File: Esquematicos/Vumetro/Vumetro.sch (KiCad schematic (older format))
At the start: 14 parts

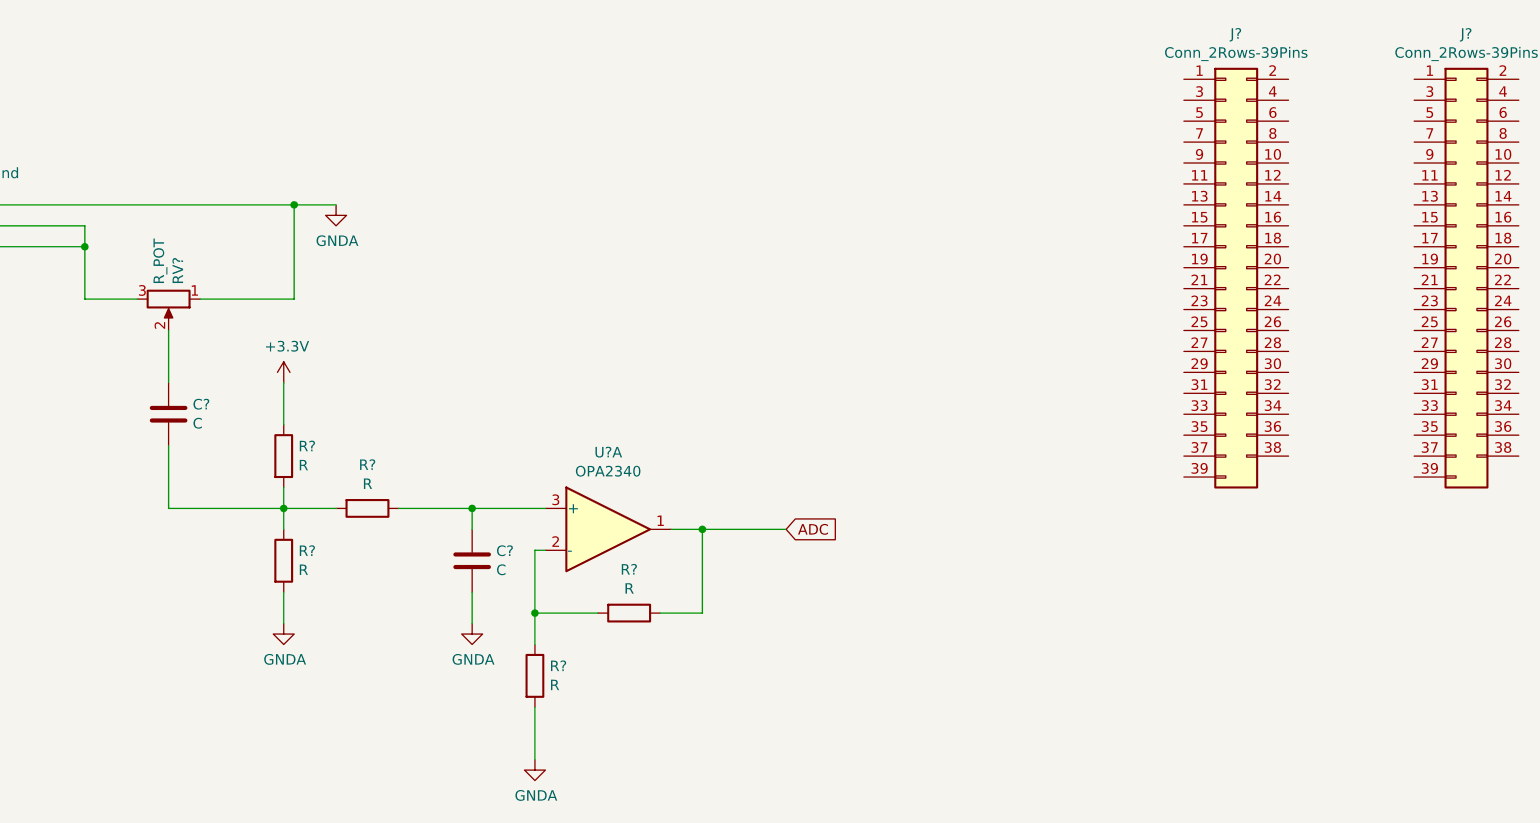
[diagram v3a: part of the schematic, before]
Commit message: Se agrega simulacion de esquematico
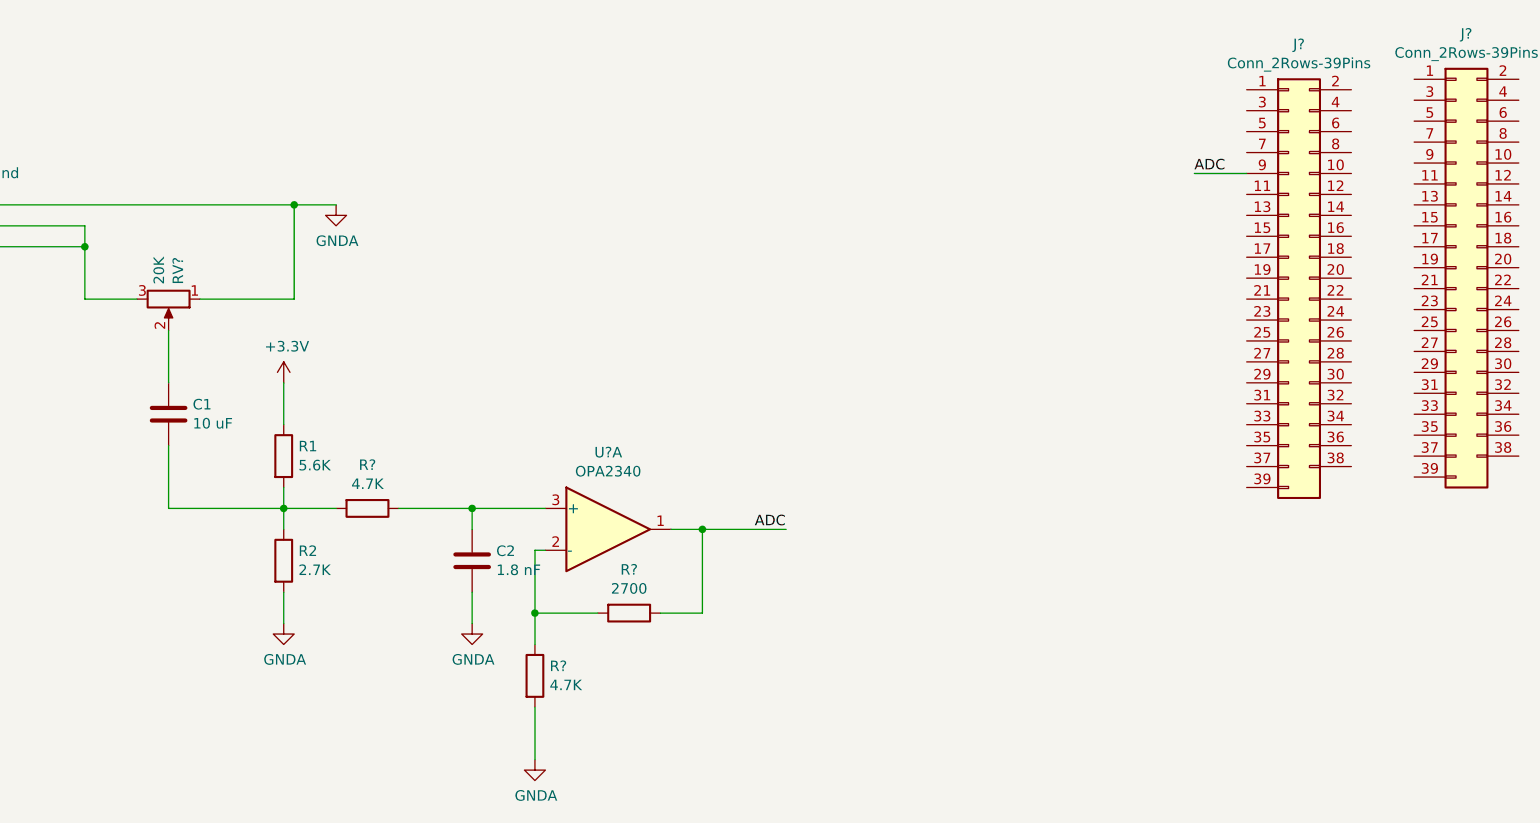
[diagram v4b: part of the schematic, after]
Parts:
- C1: renamed from C?; value C -> 10 uF
- C2: renamed from C?; value C -> 1.8 nF
- R1: renamed from R?; value R -> 5.6K
- R2: renamed from R?; value R -> 2.7K
- R? (x2): value R -> 4.7K
- R?: value R -> 2700
- RV?: value R_POT -> 20K
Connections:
- wire segments 30 -> 31
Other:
- moved on the sheet: J?
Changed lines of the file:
@@
 EESchema Schematic File Version 4
 LIBS:Vumetro-cache
-EELAYER 26 0
+EELAYER 29 0
 EELAYER END
 $Descr A4 11693 8268
@@
 $EndDescr
 $Comp
-L Device:R R?
+L Device:R R1
 U 1 1 5BD08240
 P 3400 2900
-F 0 "R?" H 3470 2946 50  0000 L CNN
-F 1 "R" H 3470 2855 50  0000 L CNN
+F 0 "R1" H 3470 2946 50  0000 L CNN
+F 1 "5.6K" H 3470 2855 50  0000 L CNN
 F 2 "" V 3330 2900 50  0001 C CNN
 F 3 "~" H 3400 2900 50  0001 C CNN
@@
 $EndComp
 $Comp
-L Device:R R?
+L Device:R R2
 U 1 1 5BD082FA
 P 3400 3400
-F 0 "R?" H 3470 3446 50  0000 L CNN
-F 1 "R" H 3470 3355 50  0000 L CNN
+F 0 "R2" H 3470 3446 50  0000 L CNN
+F 1 "2.7K" H 3470 3355 50  0000 L CNN
 F 2 "" V 3330 3400 50  0001 C CNN
 F 3 "~" H 3400 3400 50  0001 C CNN
@@
 $EndComp
 $Comp
-L power:+3.3V #PWR?
+L power:+3.3V #PWR0101
 U 1 1 5BD083BF
 P 3400 2550
-F 0 "#PWR?" H 3400 2400 50  0001 C CNN
+F 0 "#PWR0101" H 3400 2400 50  0001 C CNN
 F 1 "+3.3V" H 3415 2723 50  0000 C CNN
 F 2 "" H 3400 2550 50  0001 C CNN
@@
 $EndComp
 $Comp
-L power:GNDA #PWR?
+L power:GNDA #PWR0102
 U 1 1 5BD08B01
 P 3650 1700
-F 0 "#PWR?" H 3650 1450 50  0001 C CNN
+F 0 "#PWR0102" H 3650 1450 50  0001 C CNN
 F 1 "GNDA" H 3655 1527 50  0000 C CNN
 F 2 "" H 3650 1700 50  0001 C CNN
@@
 P 2850 2150
 F 0 "RV?" H 2780 2196 50  0000 R CNN
-F 1 "R_POT" H 2780 2105 50  0000 R CNN
+F 1 "20K" H 2780 2105 50  0000 R CNN
 F 2 "" H 2850 2150 50  0001 C CNN
 F 3 "~" H 2850 2150 50  0001 C CNN
@@
 Connection ~ 3400 3150
 $Comp
-L power:GNDA #PWR?
+L power:GNDA #PWR0103
 U 1 1 5BD0D7F2
 P 3400 3700
-F 0 "#PWR?" H 3400 3450 50  0001 C CNN
+F 0 "#PWR0103" H 3400 3450 50  0001 C CNN
 F 1 "GNDA" H 3405 3527 50  0000 C CNN
 F 2 "" H 3400 3700 50  0001 C CNN
@@
 $EndComp
 $Comp
-L Device:C C?
+L Device:C C2
 U 1 1 5BD1B29A
 P 4300 3400
-F 0 "C?" H 4415 3446 50  0000 L CNN
-F 1 "C" H 4415 3355 50  0000 L CNN
+F 0 "C2" H 4415 3446 50  0000 L CNN
+F 1 "1.8 nF" H 4415 3355 50  0000 L CNN
 F 2 "" H 4338 3250 50  0001 C CNN
 F 3 "~" H 4300 3400 50  0001 C CNN
@@
 $EndComp
 $Comp
-L power:GNDA #PWR?
+L power:GNDA #PWR0104
 U 1 1 5BD1B343
 P 4300 3700
-F 0 "#PWR?" H 4300 3450 50  0001 C CNN
+F 0 "#PWR0104" H 4300 3450 50  0001 C CNN
 F 1 "GNDA" H 4305 3527 50  0000 C CNN
 F 2 "" H 4300 3700 50  0001 C CNN
@@
 P 3800 3150
 F 0 "R?" V 3593 3150 50  0000 C CNN
-F 1 "R" V 3684 3150 50  0000 C CNN
+F 1 "4.7K" V 3684 3150 50  0000 C CNN
 F 2 "" V 3730 3150 50  0001 C CNN
 F 3 "~" H 3800 3150 50  0001 C CNN
@@
 Wire Wire Line
 	4300 3150 4300 3250
-Text GLabel 5800 3250 2    50   Input ~ 0
-ADC
 Wire Wire Line
 	3400 3550 3400 3700
@@
 L Connector_Generic:Conn_2Rows-39Pins J?
 U 1 1 5BD1C88D
-P 7900 2000
-F 0 "J?" H 7950 3117 50  0000 C CNN
-F 1 "Conn_2Rows-39Pins" H 7950 3026 50  0000 C CNN
-F 2 "" H 7900 2000 50  0001 C CNN
-F 3 "~" H 7900 2000 50  0001 C CNN
-	1    7900 2000
+P 8200 2050
+F 0 "J?" H 8250 3167 50  0000 C CNN
+F 1 "Conn_2Rows-39Pins" H 8250 3076 50  0000 C CNN
+F 2 "" H 8200 2050 50  0001 C CNN
+F 3 "~" H 8200 2050 50  0001 C CNN
+	1    8200 2050
 	1    0    0    -1
 $EndComp
@@
 P 4600 3950
 F 0 "R?" H 4670 3996 50  0000 L CNN
-F 1 "R" H 4670 3905 50  0000 L CNN
+F 1 "4.7K" H 4670 3905 50  0000 L CNN
 F 2 "" V 4530 3950 50  0001 C CNN
 F 3 "~" H 4600 3950 50  0001 C CNN
@@
 P 5050 3650
 F 0 "R?" V 4843 3650 50  0000 C CNN
-F 1 "R" V 4934 3650 50  0000 C CNN
+F 1 "2700" V 4934 3650 50  0000 C CNN
 F 2 "" V 4980 3650 50  0001 C CNN
 F 3 "~" H 5050 3650 50  0001 C CNN
@@
 	5400 3250 5250 3250
 $Comp
-L power:GNDA #PWR?
+L power:GNDA #PWR0105
 U 1 1 5BD20C9D
 P 4600 4350
-F 0 "#PWR?" H 4600 4100 50  0001 C CNN
+F 0 "#PWR0105" H 4600 4100 50  0001 C CNN
 F 1 "GNDA" H 4605 4177 50  0000 C CNN
 F 2 "" H 4600 4350 50  0001 C CNN
@@
 	4600 4100 4600 4350
 $Comp
-L Device:C C?
+L Device:C C1
 U 1 1 5BD214BE
 P 2850 2700
-F 0 "C?" H 2965 2746 50  0000 L CNN
-F 1 "C" H 2965 2655 50  0000 L CNN
+F 0 "C1" H 2965 2746 50  0000 L CNN
+F 1 "10 uF" H 2965 2655 50  0000 L CNN
 F 2 "" H 2888 2550 50  0001 C CNN
 F 3 "~" H 2850 2700 50  0001 C CNN
@@
 	5400 3250 5800 3250
 Connection ~ 5400 3250
+Text Label 5650 3250 0    50   ~ 0
+ADC
+Wire Wire Line
+	8000 1550 7750 1550
+Text Label 7750 1550 0    50   ~ 0
+ADC
 $EndSCHEMATC

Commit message: actualización esquemáticoc
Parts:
- removed J? (x2): Conn_2Rows-39Pins, symbol Connector_Generic:Conn_2Rows-39Pins
- removed U?: MatrixLed8x8, symbol vumetro:MatrixLed8x8
- U?: symbol vumetro:MAX7219 -> Vumetro-rescue:MAX7219-vumetro
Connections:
- net labels added: 3V3, ADC_CH1, ADC_CH2, ADC_CH3, DAC, GND, LOAD_CS, VDDA
- wire segments 31 -> 62
- no-connect marks 0 -> 71
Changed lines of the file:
@@
 EESchema Schematic File Version 4
 LIBS:Vumetro-cache
-EELAYER 29 0
+EELAYER 26 0
 EELAYER END
 $Descr A4 11693 8268
@@
 Wire Wire Line
 	3450 1700 3650 1700
-$Comp
-L vumetro:MAX7219 U?
-U 1 1 5BD0C6D8
-P 10150 1900
-F 0 "U?" H 10150 2065 50  0000 C CNN
-F 1 "MAX7219" H 10150 1974 50  0000 C CNN
-F 2 "" H 10150 2100 50  0001 C CNN
-F 3 "" H 10150 2100 50  0001 C CNN
-	1    10150 1900
-	1    0    0    -1
-$EndComp
 Wire Wire Line
 	3400 3050 3400 3150
@@
 	3400 3550 3400 3700
 $Comp
-L vumetro:MatrixLed8x8 U?
-U 1 1 5BD1C474
-P 10100 450
-F 0 "U?" H 10578 -229 50  0000 L CNN
-F 1 "MatrixLed8x8" H 10578 -320 50  0000 L CNN
-F 2 "" H 10000 450 50  0001 C CNN
-F 3 "" H 10000 450 50  0001 C CNN
-	1    10100 450
-	1    0    0    -1
-$EndComp
-$Comp
-L Connector_Generic:Conn_2Rows-39Pins J?
-U 1 1 5BD1C88D
-P 8200 2050
-F 0 "J?" H 8250 3167 50  0000 C CNN
-F 1 "Conn_2Rows-39Pins" H 8250 3076 50  0000 C CNN
-F 2 "" H 8200 2050 50  0001 C CNN
-F 3 "~" H 8200 2050 50  0001 C CNN
-	1    8200 2050
-	1    0    0    -1
-$EndComp
-$Comp
-L Connector_Generic:Conn_2Rows-39Pins J?
-U 1 1 5BD1CE86
-P 9000 2000
-F 0 "J?" H 9050 3117 50  0000 C CNN
-F 1 "Conn_2Rows-39Pins" H 9050 3026 50  0000 C CNN
-F 2 "" H 9000 2000 50  0001 C CNN
-F 3 "~" H 9000 2000 50  0001 C CNN
-	1    9000 2000
-	1    0    0    -1
-$EndComp
-$Comp
 L Amplifier_Operational:OPA2340 U?
 U 1 1 5BD1E25D
@@
 ADC
 Wire Wire Line
-	8000 1550 7750 1550
-Text Label 7750 1550 0    50   ~ 0
-ADC
+	8050 2400 7800 2400
+Text Label 7800 2400 0    50   ~ 0
+3V3
+Wire Wire Line
+	8050 2500 7800 2500
+Text Label 7800 2500 0    50   ~ 0
+GND
+NoConn ~ 8050 4300
+NoConn ~ 8050 4200
+NoConn ~ 8050 4100
+NoConn ~ 8050 4000
+NoConn ~ 8050 3900
+NoConn ~ 8050 3800
+NoConn ~ 8050 3700
+NoConn ~ 8050 3600
+NoConn ~ 8050 3500
+NoConn ~ 8050 3400
+NoConn ~ 8050 3300
+NoConn ~ 8050 3200
+NoConn ~ 8050 3100
+NoConn ~ 8050 3000
+NoConn ~ 8050 2900
+NoConn ~ 8550 4200
+Text Label 9300 3100 0    50   ~ 0
+DAC
+NoConn ~ 8050 2800
+NoConn ~ 8050 2700
+NoConn ~ 8050 2600
+Text Label 9300 3200 0    50   ~ 0
+VDDA
+Text Label 9300 2800 0    50   ~ 0
+ADC_CH3
+Text Label 9300 2900 0    50   ~ 0
+ADC_CH2
+Text Label 9300 3000 0    50   ~ 0
+ADC_CH1
+Wire Wire Line
+	9300 2800 9700 2800
+Wire Wire Line
+	9300 2900 9700 2900
+Wire Wire Line
+	9300 3000 9700 3000
+Wire Wire Line
+	9300 3100 9700 3100
+Wire Wire Line
+	9300 3200 9700 3200
+NoConn ~ 9700 2500
+NoConn ~ 9700 2400
+NoConn ~ 9700 2600
+NoConn ~ 9700 2700
+NoConn ~ 10200 2400
+NoConn ~ 10200 2500
+NoConn ~ 10200 2600
+NoConn ~ 10200 2700
+NoConn ~ 10200 2800
+NoConn ~ 10200 2900
+NoConn ~ 10200 3000
+NoConn ~ 10200 3100
+NoConn ~ 10200 3200
+NoConn ~ 10200 3300
+NoConn ~ 10200 3400
+NoConn ~ 10200 3500
+NoConn ~ 10200 3600
+NoConn ~ 10200 3700
+NoConn ~ 10200 3800
+NoConn ~ 10200 3900
+NoConn ~ 10200 4000
+NoConn ~ 10200 4100
+NoConn ~ 10200 4200
+NoConn ~ 9700 4300
+NoConn ~ 9700 4200
+NoConn ~ 9700 4100
+NoConn ~ 9700 4000
+NoConn ~ 9700 3900
+NoConn ~ 9700 3800
+NoConn ~ 9700 3700
+NoConn ~ 9700 3600
+NoConn ~ 9700 3500
+NoConn ~ 9700 3400
+NoConn ~ 9700 3300
+$Comp
+L Vumetro-rescue:MAX7219-vumetro U?
+U 1 1 5BD0C6D8
+P 2500 5900
+F 0 "U?" H 2500 6065 50  0000 C CNN
+F 1 "MAX7219" H 2500 5974 50  0000 C CNN
+F 2 "" H 2500 6100 50  0001 C CNN
+F 3 "" H 2500 6100 50  0001 C CNN
+	1    2500 5900
+	1    0    0    -1
+$EndComp
+NoConn ~ 8550 2400
+NoConn ~ 8550 2500
+NoConn ~ 8550 2600
+NoConn ~ 8550 2700
+NoConn ~ 8550 2800
+NoConn ~ 8550 2900
+NoConn ~ 8550 3000
+NoConn ~ 8550 3100
+NoConn ~ 8550 3200
+NoConn ~ 8550 3300
+NoConn ~ 8550 3400
+NoConn ~ 8550 3500
+NoConn ~ 8550 3600
+NoConn ~ 8550 3700
+NoConn ~ 8550 3800
+NoConn ~ 8550 3900
+NoConn ~ 8550 4000
+NoConn ~ 8550 4100
+Wire Wire Line
+	2000 6100 1850 6100
+Wire Wire Line
+	1850 6100 1850 5400
+Wire Wire Line
+	1850 5400 3350 5400
+Wire Wire Line
+	2000 6200 1750 6200
+Wire Wire Line
+	1750 6200 1750 5300
+Wire Wire Line
+	1750 5300 3350 5300
+Wire Wire Line
+	2000 6400 1650 6400
+Wire Wire Line
+	1650 6400 1650 5200
+Wire Wire Line
+	1650 5200 3350 5200
+Wire Wire Line
+	2000 6500 1550 6500
+Wire Wire Line
+	1550 6500 1550 5100
+Wire Wire Line
+	1550 5100 3350 5100
+Wire Wire Line
+	2000 6600 1450 6600
+Wire Wire Line
+	1450 6600 1450 5000
+Wire Wire Line
+	1450 5000 3350 5000
+Wire Wire Line
+	2000 6700 1350 6700
+Wire Wire Line
+	1350 6700 1350 4900
+Wire Wire Line
+	1350 4900 3350 4900
+Wire Wire Line
+	2000 6900 1250 6900
+Wire Wire Line
+	1250 6900 1250 4800
+Wire Wire Line
+	1250 4800 3350 4800
+Wire Wire Line
+	2000 7000 1150 7000
+Wire Wire Line
+	1150 7000 1150 4700
+Wire Wire Line
+	1150 4700 3350 4700
+Wire Wire Line
+	2000 7100 1650 7100
+Text Label 1650 7100 0    50   ~ 0
+LOAD_CS
 $EndSCHEMATC

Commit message: Revert "actualización esquemáticoc"
This reverts commit c61605e0acc8271fae062afea902648c4f968452.
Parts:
- added J? (x2): Conn_2Rows-39Pins, symbol Connector_Generic:Conn_2Rows-39Pins
- added U?: MatrixLed8x8, symbol vumetro:MatrixLed8x8
- U?: symbol Vumetro-rescue:MAX7219-vumetro -> vumetro:MAX7219
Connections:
- net labels removed: 3V3, ADC_CH1, ADC_CH2, ADC_CH3, DAC, GND, LOAD_CS, VDDA
- wire segments 62 -> 31
- no-connect marks 71 -> 0
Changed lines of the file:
@@
 EESchema Schematic File Version 4
 LIBS:Vumetro-cache
-EELAYER 26 0
+EELAYER 29 0
 EELAYER END
 $Descr A4 11693 8268
@@
 Wire Wire Line
 	3450 1700 3650 1700
+$Comp
+L vumetro:MAX7219 U?
+U 1 1 5BD0C6D8
+P 10150 1900
+F 0 "U?" H 10150 2065 50  0000 C CNN
+F 1 "MAX7219" H 10150 1974 50  0000 C CNN
+F 2 "" H 10150 2100 50  0001 C CNN
+F 3 "" H 10150 2100 50  0001 C CNN
+	1    10150 1900
+	1    0    0    -1
+$EndComp
 Wire Wire Line
 	3400 3050 3400 3150
@@
 	3400 3550 3400 3700
 $Comp
+L vumetro:MatrixLed8x8 U?
+U 1 1 5BD1C474
+P 10100 450
+F 0 "U?" H 10578 -229 50  0000 L CNN
+F 1 "MatrixLed8x8" H 10578 -320 50  0000 L CNN
+F 2 "" H 10000 450 50  0001 C CNN
+F 3 "" H 10000 450 50  0001 C CNN
+	1    10100 450
+	1    0    0    -1
+$EndComp
+$Comp
+L Connector_Generic:Conn_2Rows-39Pins J?
+U 1 1 5BD1C88D
+P 8200 2050
+F 0 "J?" H 8250 3167 50  0000 C CNN
+F 1 "Conn_2Rows-39Pins" H 8250 3076 50  0000 C CNN
+F 2 "" H 8200 2050 50  0001 C CNN
+F 3 "~" H 8200 2050 50  0001 C CNN
+	1    8200 2050
+	1    0    0    -1
+$EndComp
+$Comp
+L Connector_Generic:Conn_2Rows-39Pins J?
+U 1 1 5BD1CE86
+P 9000 2000
+F 0 "J?" H 9050 3117 50  0000 C CNN
+F 1 "Conn_2Rows-39Pins" H 9050 3026 50  0000 C CNN
+F 2 "" H 9000 2000 50  0001 C CNN
+F 3 "~" H 9000 2000 50  0001 C CNN
+	1    9000 2000
+	1    0    0    -1
+$EndComp
+$Comp
 L Amplifier_Operational:OPA2340 U?
 U 1 1 5BD1E25D
@@
 ADC
 Wire Wire Line
-	8050 2400 7800 2400
-Text Label 7800 2400 0    50   ~ 0
-3V3
-Wire Wire Line
-	8050 2500 7800 2500
-Text Label 7800 2500 0    50   ~ 0
-GND
-NoConn ~ 8050 4300
-NoConn ~ 8050 4200
-NoConn ~ 8050 4100
-NoConn ~ 8050 4000
-NoConn ~ 8050 3900
-NoConn ~ 8050 3800
-NoConn ~ 8050 3700
-NoConn ~ 8050 3600
-NoConn ~ 8050 3500
-NoConn ~ 8050 3400
-NoConn ~ 8050 3300
-NoConn ~ 8050 3200
-NoConn ~ 8050 3100
-NoConn ~ 8050 3000
-NoConn ~ 8050 2900
-NoConn ~ 8550 4200
-Text Label 9300 3100 0    50   ~ 0
-DAC
-NoConn ~ 8050 2800
-NoConn ~ 8050 2700
-NoConn ~ 8050 2600
-Text Label 9300 3200 0    50   ~ 0
-VDDA
-Text Label 9300 2800 0    50   ~ 0
-ADC_CH3
-Text Label 9300 2900 0    50   ~ 0
-ADC_CH2
-Text Label 9300 3000 0    50   ~ 0
-ADC_CH1
-Wire Wire Line
-	9300 2800 9700 2800
-Wire Wire Line
-	9300 2900 9700 2900
-Wire Wire Line
-	9300 3000 9700 3000
-Wire Wire Line
-	9300 3100 9700 3100
-Wire Wire Line
-	9300 3200 9700 3200
-NoConn ~ 9700 2500
-NoConn ~ 9700 2400
-NoConn ~ 9700 2600
-NoConn ~ 9700 2700
-NoConn ~ 10200 2400
-NoConn ~ 10200 2500
-NoConn ~ 10200 2600
-NoConn ~ 10200 2700
-NoConn ~ 10200 2800
-NoConn ~ 10200 2900
-NoConn ~ 10200 3000
-NoConn ~ 10200 3100
-NoConn ~ 10200 3200
-NoConn ~ 10200 3300
-NoConn ~ 10200 3400
-NoConn ~ 10200 3500
-NoConn ~ 10200 3600
-NoConn ~ 10200 3700
-NoConn ~ 10200 3800
-NoConn ~ 10200 3900
-NoConn ~ 10200 4000
-NoConn ~ 10200 4100
-NoConn ~ 10200 4200
-NoConn ~ 9700 4300
-NoConn ~ 9700 4200
-NoConn ~ 9700 4100
-NoConn ~ 9700 4000
-NoConn ~ 9700 3900
-NoConn ~ 9700 3800
-NoConn ~ 9700 3700
-NoConn ~ 9700 3600
-NoConn ~ 9700 3500
-NoConn ~ 9700 3400
-NoConn ~ 9700 3300
-$Comp
-L Vumetro-rescue:MAX7219-vumetro U?
-U 1 1 5BD0C6D8
-P 2500 5900
-F 0 "U?" H 2500 6065 50  0000 C CNN
-F 1 "MAX7219" H 2500 5974 50  0000 C CNN
-F 2 "" H 2500 6100 50  0001 C CNN
-F 3 "" H 2500 6100 50  0001 C CNN
-	1    2500 5900
-	1    0    0    -1
-$EndComp
-NoConn ~ 8550 2400
-NoConn ~ 8550 2500
-NoConn ~ 8550 2600
-NoConn ~ 8550 2700
-NoConn ~ 8550 2800
-NoConn ~ 8550 2900
-NoConn ~ 8550 3000
-NoConn ~ 8550 3100
-NoConn ~ 8550 3200
-NoConn ~ 8550 3300
-NoConn ~ 8550 3400
-NoConn ~ 8550 3500
-NoConn ~ 8550 3600
-NoConn ~ 8550 3700
-NoConn ~ 8550 3800
-NoConn ~ 8550 3900
-NoConn ~ 8550 4000
-NoConn ~ 8550 4100
-Wire Wire Line
-	2000 6100 1850 6100
-Wire Wire Line
-	1850 6100 1850 5400
-Wire Wire Line
-	1850 5400 3350 5400
-Wire Wire Line
-	2000 6200 1750 6200
-Wire Wire Line
-	1750 6200 1750 5300
-Wire Wire Line
-	1750 5300 3350 5300
-Wire Wire Line
-	2000 6400 1650 6400
-Wire Wire Line
-	1650 6400 1650 5200
-Wire Wire Line
-	1650 5200 3350 5200
-Wire Wire Line
-	2000 6500 1550 6500
-Wire Wire Line
-	1550 6500 1550 5100
-Wire Wire Line
-	1550 5100 3350 5100
-Wire Wire Line
-	2000 6600 1450 6600
-Wire Wire Line
-	1450 6600 1450 5000
-Wire Wire Line
-	1450 5000 3350 5000
-Wire Wire Line
-	2000 6700 1350 6700
-Wire Wire Line
-	1350 6700 1350 4900
-Wire Wire Line
-	1350 4900 3350 4900
-Wire Wire Line
-	2000 6900 1250 6900
-Wire Wire Line
-	1250 6900 1250 4800
-Wire Wire Line
-	1250 4800 3350 4800
-Wire Wire Line
-	2000 7000 1150 7000
-Wire Wire Line
-	1150 7000 1150 4700
-Wire Wire Line
-	1150 4700 3350 4700
-Wire Wire Line
-	2000 7100 1650 7100
-Text Label 1650 7100 0    50   ~ 0
-LOAD_CS
+	8000 1550 7750 1550
+Text Label 7750 1550 0    50   ~ 0
+ADC
 $EndSCHEMATC

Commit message: se agrega archivos
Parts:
- removed J? (x2): Conn_2Rows-39Pins, symbol Connector_Generic:Conn_2Rows-39Pins
- removed U?: MatrixLed8x8, symbol vumetro:MatrixLed8x8
- added U? (x2): conn_pin8, symbol vumetro:conn_pin8
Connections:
- wire segments 31 -> 30
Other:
- moved on the sheet: U?
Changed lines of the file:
@@
 L vumetro:MAX7219 U?
 U 1 1 5BD0C6D8
-P 10150 1900
-F 0 "U?" H 10150 2065 50  0000 C CNN
-F 1 "MAX7219" H 10150 1974 50  0000 C CNN
-F 2 "" H 10150 2100 50  0001 C CNN
-F 3 "" H 10150 2100 50  0001 C CNN
-	1    10150 1900
+P 2100 5400
+F 0 "U?" H 2100 5565 50  0000 C CNN
+F 1 "MAX7219" H 2100 5474 50  0000 C CNN
+F 2 "" H 2100 5600 50  0001 C CNN
+F 3 "" H 2100 5600 50  0001 C CNN
+	1    2100 5400
 	1    0    0    -1
 $EndComp
@@
 Wire Wire Line
 	3400 3550 3400 3700
-$Comp
-L vumetro:MatrixLed8x8 U?
-U 1 1 5BD1C474
-P 10100 450
-F 0 "U?" H 10578 -229 50  0000 L CNN
-F 1 "MatrixLed8x8" H 10578 -320 50  0000 L CNN
-F 2 "" H 10000 450 50  0001 C CNN
-F 3 "" H 10000 450 50  0001 C CNN
-	1    10100 450
-	1    0    0    -1
-$EndComp
-$Comp
-L Connector_Generic:Conn_2Rows-39Pins J?
-U 1 1 5BD1C88D
-P 8200 2050
-F 0 "J?" H 8250 3167 50  0000 C CNN
-F 1 "Conn_2Rows-39Pins" H 8250 3076 50  0000 C CNN
-F 2 "" H 8200 2050 50  0001 C CNN
-F 3 "~" H 8200 2050 50  0001 C CNN
-	1    8200 2050
-	1    0    0    -1
-$EndComp
-$Comp
-L Connector_Generic:Conn_2Rows-39Pins J?
-U 1 1 5BD1CE86
-P 9000 2000
-F 0 "J?" H 9050 3117 50  0000 C CNN
-F 1 "Conn_2Rows-39Pins" H 9050 3026 50  0000 C CNN
-F 2 "" H 9000 2000 50  0001 C CNN
-F 3 "~" H 9000 2000 50  0001 C CNN
-	1    9000 2000
-	1    0    0    -1
-$EndComp
 $Comp
 L Amplifier_Operational:OPA2340 U?
@@
 Text Label 5650 3250 0    50   ~ 0
 ADC
-Wire Wire Line
-	8000 1550 7750 1550
-Text Label 7750 1550 0    50   ~ 0
-ADC
+$Comp
+L vumetro:conn_pin8 U?
+U 1 1 5BD8D993
+P 4000 5450
+F 0 "U?" H 3900 5550 50  0000 L CNN
+F 1 "conn_pin8" H 3850 5450 50  0000 L CNN
+F 2 "" H 4000 5450 50  0001 C CNN
+F 3 "" H 4000 5450 50  0001 C CNN
+	1    4000 5450
+	1    0    0    -1
+$EndComp
+$Comp
+L vumetro:conn_pin8 U?
+U 1 1 5BD8E115
+P 4750 5450
+F 0 "U?" H 4667 5515 50  0000 C CNN
+F 1 "conn_pin8" H 4667 5424 50  0000 C CNN
+F 2 "" H 4750 5450 50  0001 C CNN
+F 3 "" H 4750 5450 50  0001 C CNN
+	1    4750 5450
+	-1   0    0    -1
+$EndComp
 $EndSCHEMATC
